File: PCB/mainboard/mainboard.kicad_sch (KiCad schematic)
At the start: 44 parts

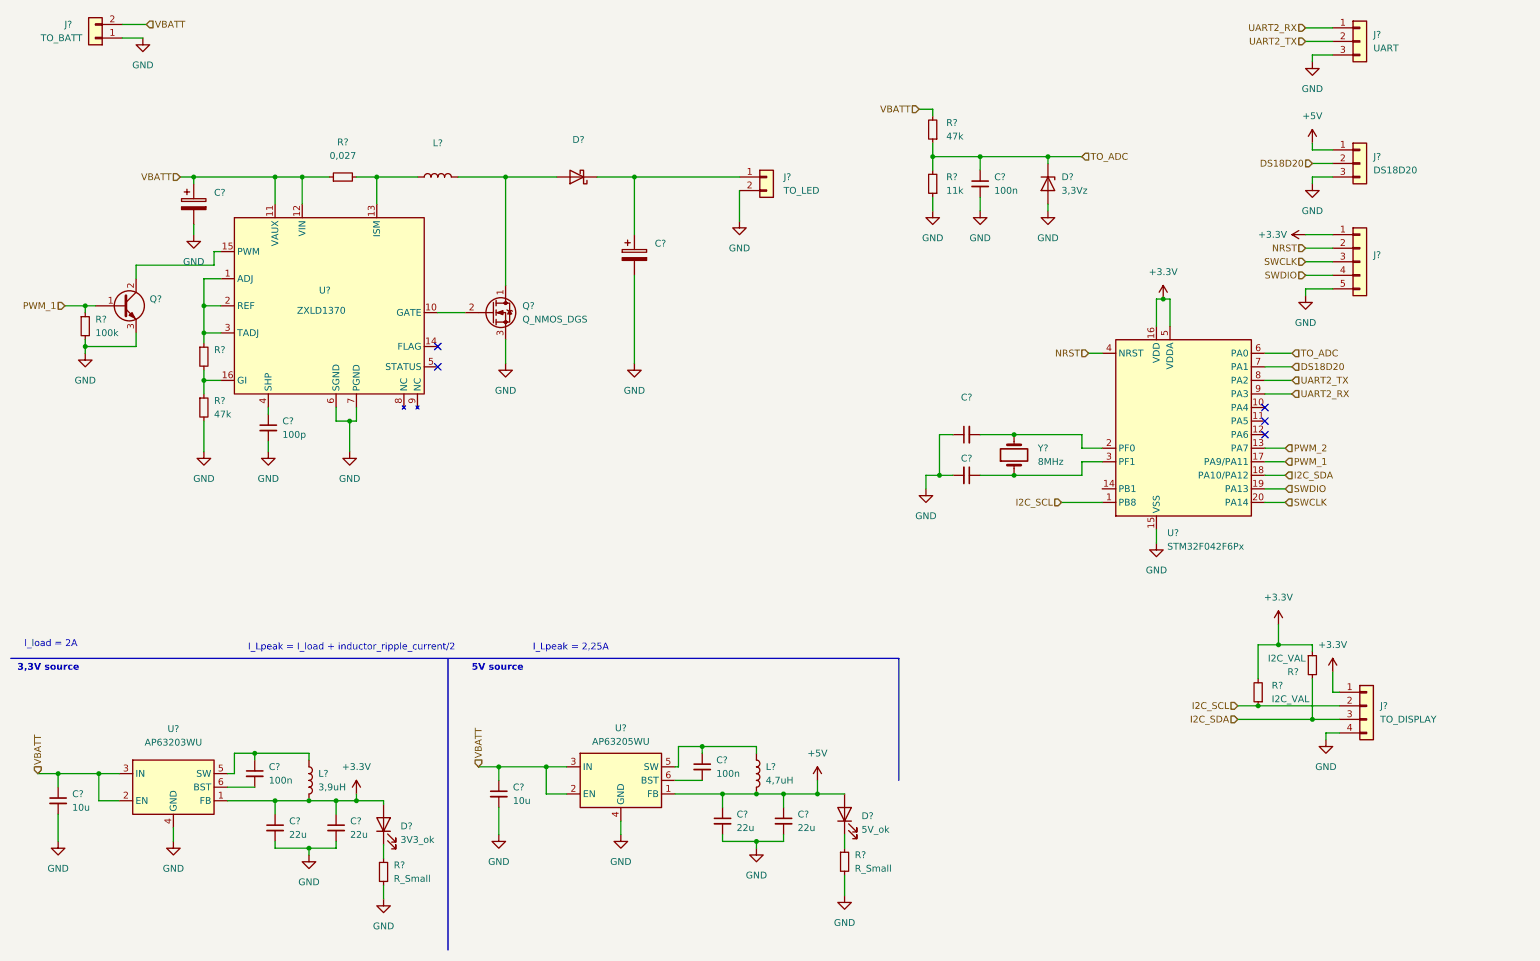
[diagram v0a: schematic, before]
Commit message: Modified calc and added TODO description to scheme
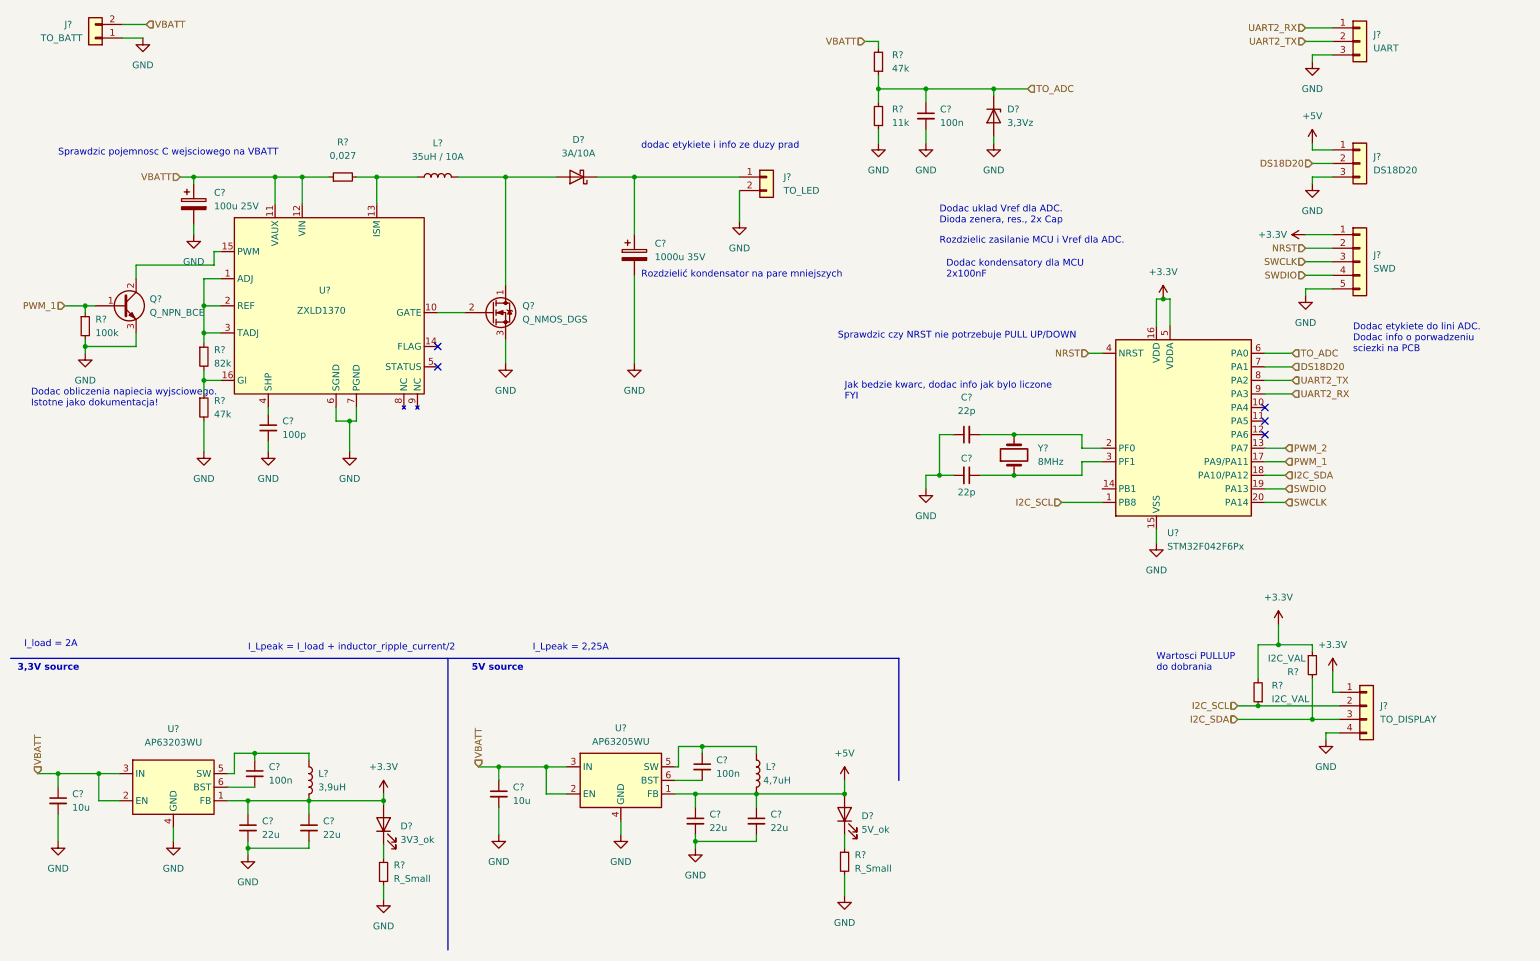
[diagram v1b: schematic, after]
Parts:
- C? (x2): value (none) -> 22p
- C?: value (none) -> 1000u 35V
- C?: value (none) -> 100u 25V
- D?: value (none) -> 3A/10A
- J?: value (none) -> SWD
- L?: value (none) -> 35uH / 10A
- Q?: value (none) -> Q_NPN_BCE
- R?: value (none) -> 82k
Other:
- note added: "Dodac etykiete do lini ADC. Dodac info o porwadzeniu sciezki na PCB"
- note added: "Dodac kondensatory dla MCU 2x100nF"
- note added: "Dodac obliczenia napiecia wyjsciowego. Istotne jako dokumentacja!"
- note added: "Dodac uklad Vref dla ADC. Dioda zenera, res., 2x Cap"
- note added: "Jak bedzie kwarc, dodac info jak bylo liczone FYI"
- note added: "Rozdzielic zasilanie MCU i Vref dla ADC."
- note added: "Rozdzielić kondensator na pare mniejszych"
- note added: "Sprawdzic czy NRST nie potrzebuje PULL UP/DOWN"
- note added: "Sprawdzic pojemnosc C wejsciowego na VBATT"
- note added: "Wartosci PULLUP do dobrania"
- note added: "dodac etykiete i info ze duzy prad"
- moved on the sheet: C?, D?, R?

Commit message: improve schematics
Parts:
- removed C? (x2): 22p, symbol Device:C_Small
- removed C?: 1000u 35V, symbol Device:C_Polarized
- removed Y?: 8MHz, symbol Device:Crystal
- added C? (x4): (no value), symbol Device:C_Polarized_Small
- added C? (x4): 100n, symbol Device:C_Small
- added D?: 3,3Vz, symbol Device:D_Zener
- added R?: (no value), symbol Device:R_Small
- D?: value 3A/10A -> (none)
- R? (x2): value I2C_VAL -> (none)
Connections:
- net +3.3V: now also C?.1, C?.1; no longer U?.5 (VDDA)
- net +5V: now also R?.2
- net GND: now also C?.2, C?.2, C?.2, C?.2, C?.2, C?.2, C?.2, C?.2, D?.2 (A)
- net at D?.1 (K), J?.1 (Pin_1): now also C?.1, C?.1, C?.1, C?.1
- new net +3.3VADC: C?.1, C?.1, D?.1 (K), R?.1, U?.5 (VDDA)
- no-connect marks 5 -> 8
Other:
- note added: "3,3Vref source"
- note added: "4x"
- note added: "Kwarc nie będzie potrzebny, Wykorzystam wewnętrzny oscylator"
- note added: "MAX 164 uA"
- note added: "MAX 21 mA"
- note added: "podobno nie potrzeba pullup'ów, ale dam footprinty na wszelki wypadek"
- note removed: "Dodac kondensatory dla MCU 2x100nF"
- note removed: "Dodac obliczenia napiecia wyjsciowego. Istotne jako dokumentacja!"
- note removed: "Dodac uklad Vref dla ADC. Dioda zenera, res., 2x Cap"
- note removed: "Jak bedzie kwarc, dodac info jak bylo liczone FYI"
- note removed: "Rozdzielic zasilanie MCU i Vref dla ADC."
- note removed: "Rozdzielić kondensator na pare mniejszych"
- note removed: "Wartosci PULLUP do dobrania"
- moved on the sheet: J?, R?

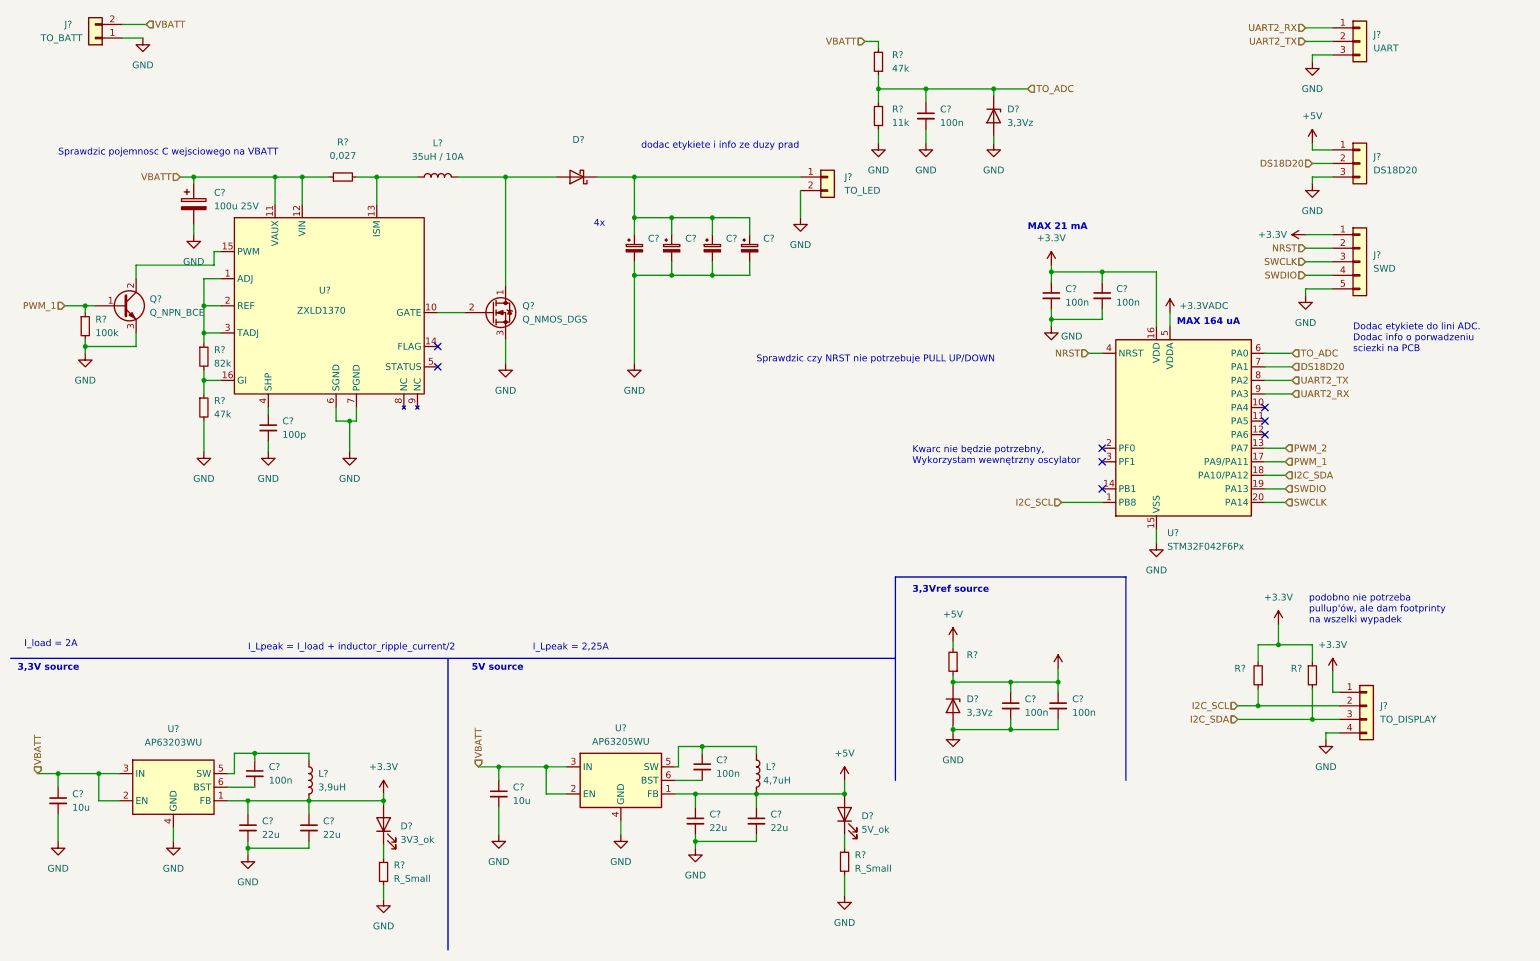
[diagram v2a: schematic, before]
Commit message: Convert Motherboard to KiCad 7.0
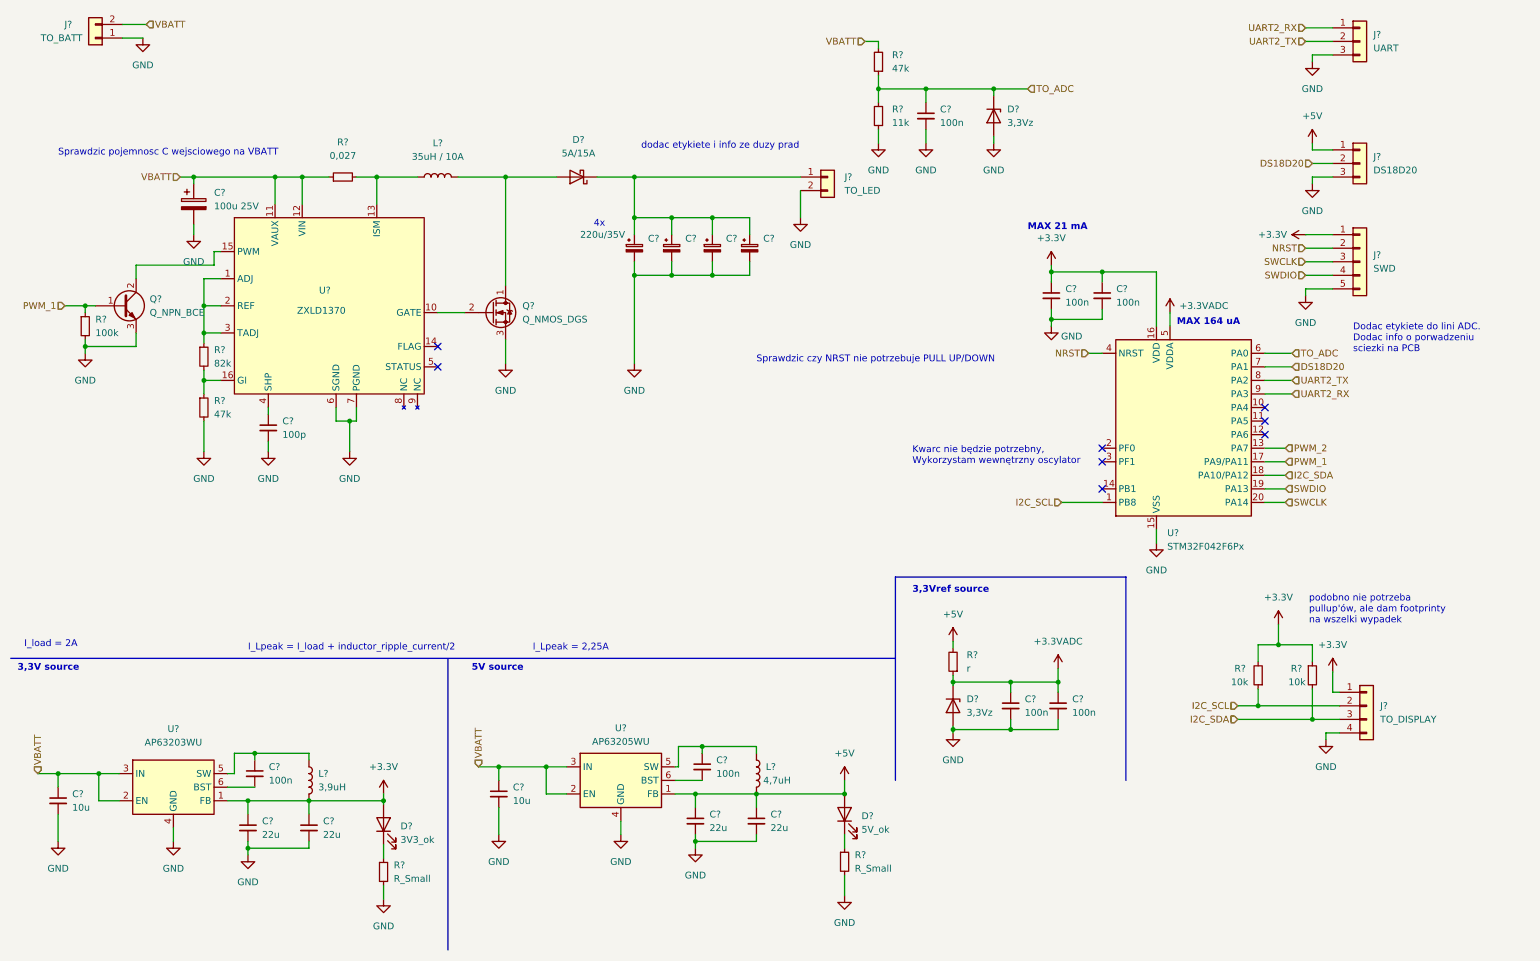
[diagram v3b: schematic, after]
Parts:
- C? (x4): value (none) -> 220u/35V
- D?: value (none) -> 5A/15A
- R? (x2): value (none) -> 10k
- R?: value (none) -> r

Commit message: Divide scheme into 2 different sheets
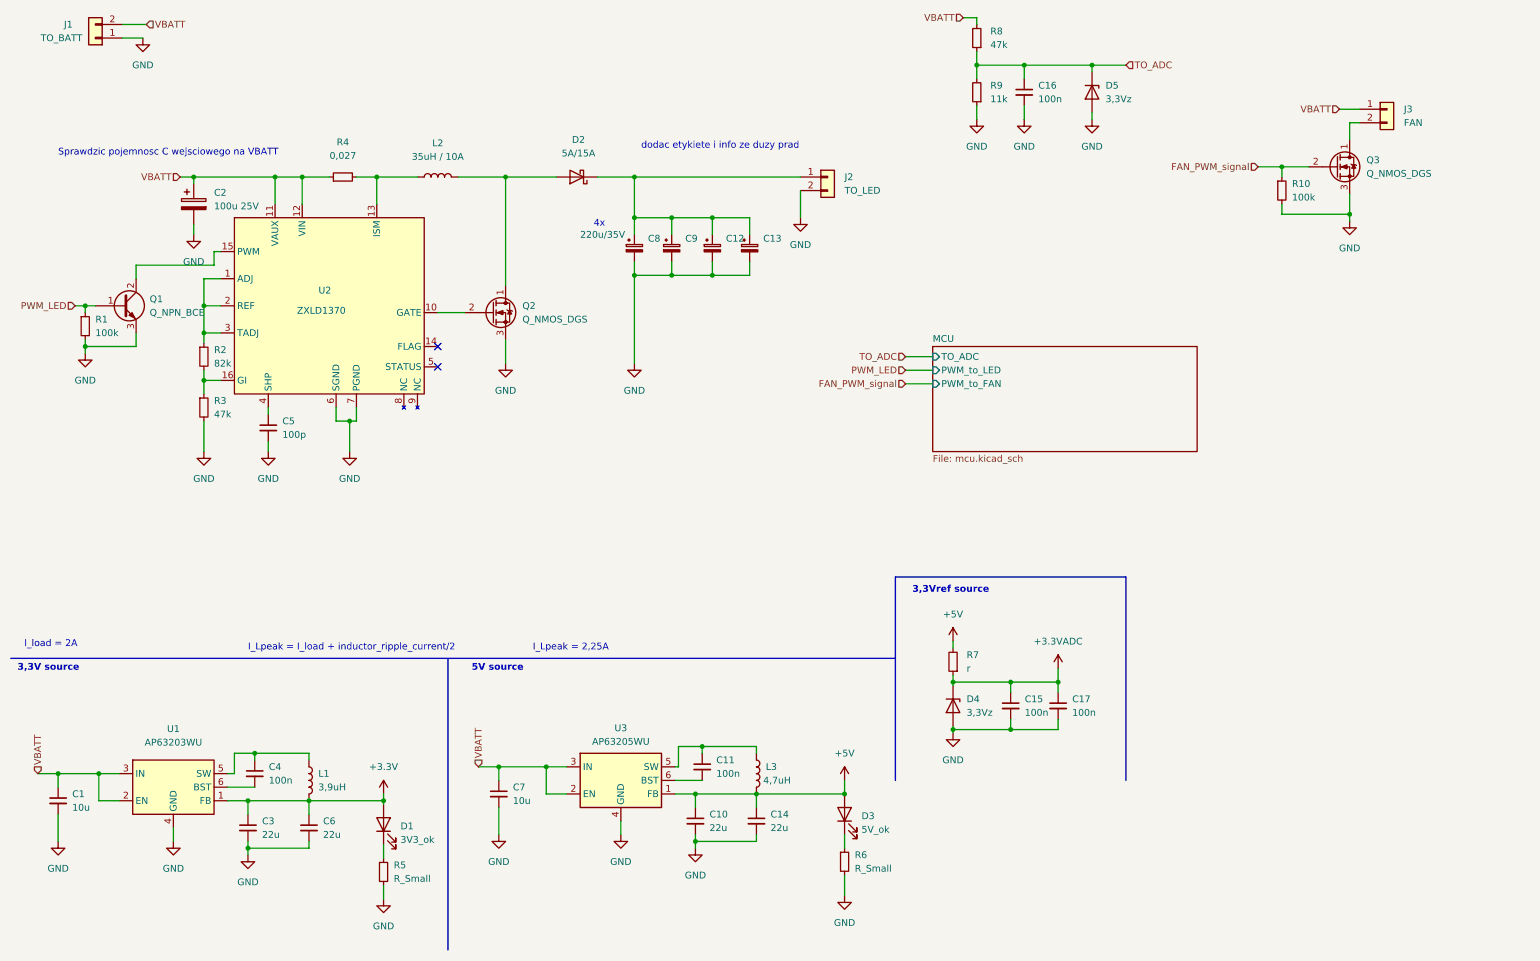
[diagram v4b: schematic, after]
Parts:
- removed C? (x2): 100n, symbol Device:C_Small
- removed J?: UART, symbol Connector_Generic:Conn_01x03
- removed J?: SWD, symbol Connector_Generic:Conn_01x05
- removed J?: TO_DISPLAY, symbol Connector_Generic:Conn_01x04
- removed J?: DS18D20, symbol Connector_Generic:Conn_01x03
- removed R? (x2): 10k, symbol Device:R_Small
- removed U?: STM32F042F6Px, Package_SO:TSSOP-20_4.4x6.5mm_P0.65mm, symbol MCU_ST_STM32F0:STM32F042F6Px
- added J3: FAN, symbol Connector_Generic:Conn_01x02
- added Q3: Q_NMOS_DGS, symbol Device:Q_NMOS_DGS
- added R10: 100k, symbol Device:R_Small
- gave numbers to parts that had none: 41
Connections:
- net GND: now also Q3.3 (S), R10.2
- net VBATT: now also J3.1 (Pin_1)
- net PWM_1 renamed PWM_LED
- new net: J3.2 (Pin_2), Q3.1 (D)
- new net FAN_PWM_signal: Q3.2 (G), R10.1
- no-connect marks 8 -> 2
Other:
- added sheet MCU (mcu.kicad_sch)
- note removed: "Dodac etykiete do lini ADC. Dodac info o porwadzeniu sciezki na PCB"
- note removed: "Kwarc nie będzie potrzebny, Wykorzystam wewnętrzny oscylator"
- note removed: "MAX 164 uA"
- note removed: "MAX 21 mA"
- note removed: "Sprawdzic czy NRST nie potrzebuje PULL UP/DOWN"
- note removed: "podobno nie potrzeba pullup'ów, ale dam footprinty na wszelki wypadek"
- moved on the sheet: C16, D5, R8, R9

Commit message: small details and sugestions
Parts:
- added Q4: Q_NMOS_DGS, symbol Device:Q_NMOS_DGS
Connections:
- net GND: no longer J2.2 (Pin_2)
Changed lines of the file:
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@@
     (stroke (width 0) (type default))
   )
-  (wire (pts (xy 159.385 55.88) (xy 159.385 60.96))
+  (wire (pts (xy 158.75 73.66) (xy 158.75 80.01))
     (stroke (width 0) (type default))
   )
@@
   )
   (wire (pts (xy 262.255 60.325) (xy 262.255 61.595))
+    (stroke (width 0) (type default))
+  )
+  (wire (pts (xy 158.75 73.66) (xy 159.385 73.66))
     (stroke (width 0) (type default))
   )
@@
     )
   )
-  (symbol (lib_id "power:GND") (at 159.385 60.96 0) (unit 1)
-    (in_bom yes) (on_board yes) (dnp no) (fields_autoplaced)
-    (property "Reference" "#PWR017" (at 159.385 67.31 0)
-      (effects (font (size 1.27 1.27)) hide)
-    )
-    (property "Value" "GND" (at 159.385 66.04 0)
-      (effects (font (size 1.27 1.27)))
-    )
-    (property "Footprint" "" (at 159.385 60.96 0)
-      (effects (font (size 1.27 1.27)) hide)
-    )
-    (property "Datasheet" "" (at 159.385 60.96 0)
+  (symbol (lib_id "power:GND") (at 158.75 80.01 0) (unit 1)
+    (in_bom yes) (on_board yes) (dnp no) (fields_autoplaced)
+    (property "Reference" "#PWR017" (at 158.75 86.36 0)
+      (effects (font (size 1.27 1.27)) hide)
+    )
+    (property "Value" "GND" (at 158.75 85.09 0)
+      (effects (font (size 1.27 1.27)))
+    )
+    (property "Footprint" "" (at 158.75 80.01 0)
+      (effects (font (size 1.27 1.27)) hide)
+    )
+    (property "Datasheet" "" (at 158.75 80.01 0)
       (effects (font (size 1.27 1.27)) hide)
     )
@@
         )
       )
+    )
+  )
+  (symbol (lib_id "Device:Q_NMOS_DGS") (at 161.29 66.04 180) (unit 1)
+    (in_bom yes) (on_board yes) (dnp no)
+    (property "Reference" "Q4" (at 154.94 64.77 0)
+      (effects (font (size 1.27 1.27)) (justify left))
+    )
+    (property "Value" "Q_NMOS_DGS" (at 179.07 71.12 0)
+      (effects (font (size 1.27 1.27)) (justify left))
+    )
+    (property "Footprint" "" (at 156.21 68.58 0)
+      (effects (font (size 1.27 1.27)) hide)
+    )
+    (property "Datasheet" "~" (at 161.29 66.04 0)
+      (effects (font (size 1.27 1.27)) hide)
+    )
+    (pin "1")
+    (pin "2")
+    (pin "3")
+    (instances
+      (project "mainboard"
+        (path "/e63e39d7-6ac0-4ffd-8aa3-1841a4541b55"
+          (reference "Q4") (unit 1)
+        )
+      )
